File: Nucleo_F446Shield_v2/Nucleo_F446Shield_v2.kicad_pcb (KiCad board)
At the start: 2 copper layers, 85 x 97.4 mm, 49 parts, among them J1 Barrel_Jack, J19 I2C3, J2 Conn_02x13_Odd_Even, J20 UART4, J21 xt60 male, J3 CAN1, J4 CAN2, SW1 SW1, SW11 DIP1, SW2 SW2, SW3 SW3, U1 NUCLEO-F446RE, U2 MP1584, U3 TJA1050, U4 TJA1050

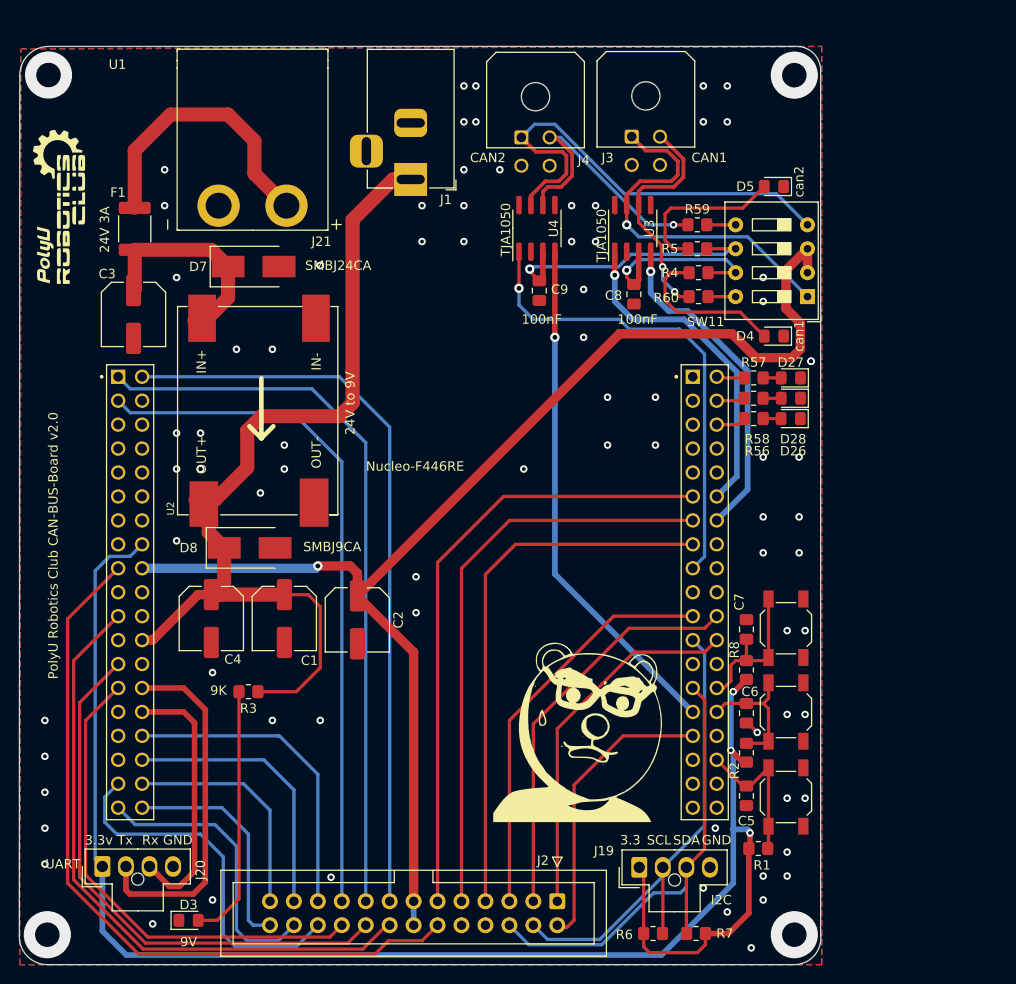
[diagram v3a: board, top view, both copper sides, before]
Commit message: added NucleoF446
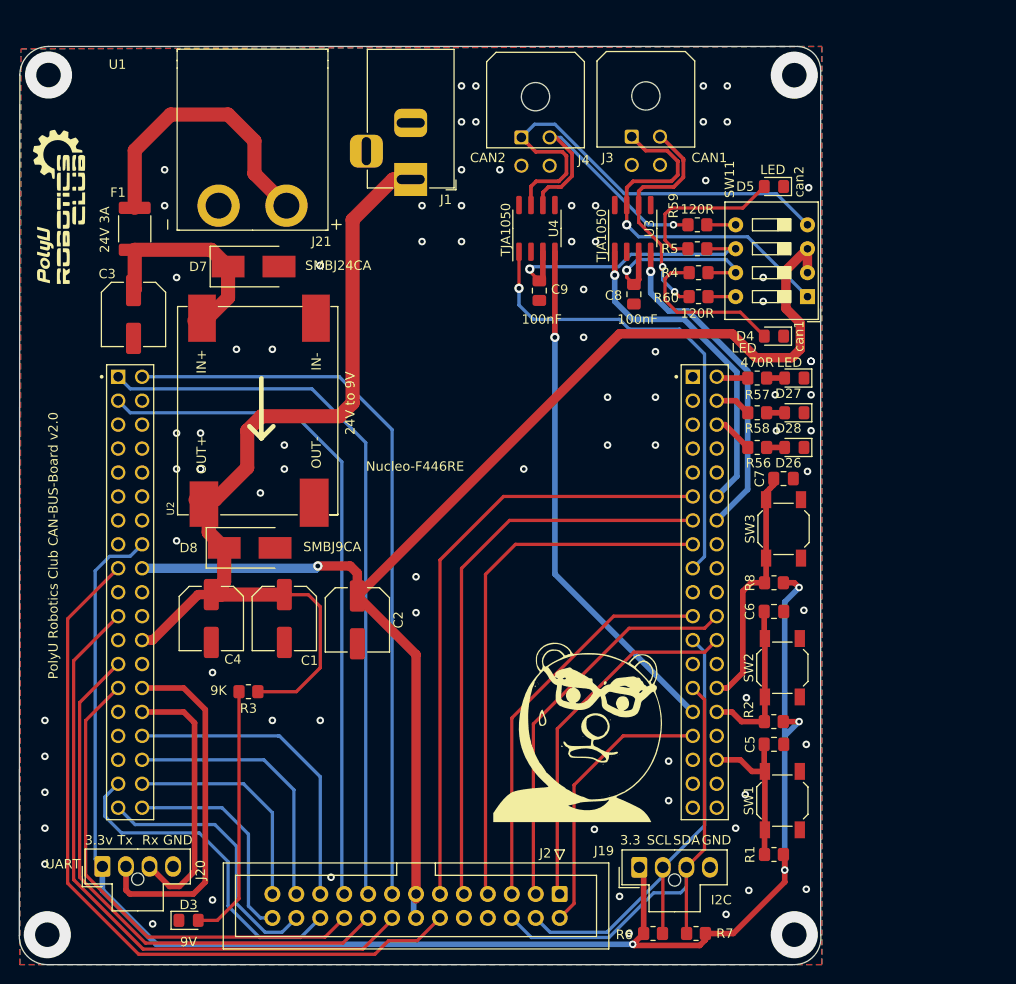
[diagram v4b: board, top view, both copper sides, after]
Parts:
- moved C7 16.5 mm to (125.3, 79.8), turned to 0 degrees
- moved C6 11.2 mm to (124.3, 93.9), turned to 0 degrees
- moved SW3 10.5 mm to (125.3, 85.1)
- moved R8 9.71 mm to (124.3, 90.8), turned to 0 degrees
- moved C5 6.19 mm to (124.3, 108.0), turned to 0 degrees
- moved SW2 4.71 mm to (125.2, 99.8)
- moved R2 4.40 mm to (124.3, 105.5), turned to 0 degrees
- moved D26 3.09 mm to (126.5, 76.5)
- moved R56 3.09 mm to (122.6, 76.5)
- moved R1 1.78 mm to (124.3, 119.6), turned to 0 degrees
- moved R58 1.59 mm to (122.6, 72.8)
- moved D28 1.58 mm to (126.5, 72.8)
- moved J2 0.81 mm to (101.6, 123.8)
- moved SW1 0.54 mm to (125.2, 113.9)
- moved D27 0.37 mm to (126.5, 69.1)
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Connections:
- J2 pad 10: unconnected-(J2-Pad10) -> GND
- J2 pad 8: unconnected-(J2-Pad8) -> GND
- U1 pad CN10_1: /PC9 -> unconnected-(U1-PadCN10_1)
- U1 pad CN10_19: /PC7 -> unconnected-(U1-PadCN10_19)
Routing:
- net /PB14: track 16.3 -> 26.5 mm
- net +3V3: track 173.5 -> 166.5 mm, vias 3 -> 4
- net /PB13: track 14.4 -> 17.2 mm
- net PC2: track 38.5 -> 35.8 mm
- net PB3: track 31.3 -> 29.5 mm
- net PC3: track 30.4 -> 28.6 mm
- net GND: track 1.64 -> 0.09 mm
- net /PC4: track 16.0 -> 17.4 mm
- net /PC5: track 3.20 -> 4.30 mm
- net PC0: track 24.1 -> 23.1 mm
- net PA9: track 43.2 -> 42.3 mm
- net /PC6: track 3.02 -> 3.83 mm
- net PB7: track 67.5 -> 68.2 mm
- net PB1: track 39.1 -> 38.4 mm
- net PB0: track 29.2 -> 28.6 mm
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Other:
- board text added: "120R"
- board text added: "470R"
- board text added: "CAN1 120R"
- board text added: "CAN1 Enable"
- board text added: "CAN2 120R"
- board text added: "CAN2 Enable"
- board text added: "LED"
- board text added: "PA0"
- board text added: "PA1"
- board text added: "PA11 PA12"
- board text added: "PA8"
- board text added: "PB4"
- board text added: "PB5 PB6"
